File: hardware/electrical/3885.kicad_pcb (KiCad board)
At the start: 4 copper layers, 33 x 77 mm, 115 parts, among them J1 USB_B_Micro, J2 TC2030, J3 Micro_SD_Card_Det1, J4 JST-PH, J5 FFC, J6 2.54mm, Q1 AO3400A, Q2 AO3400A, Q3 AO3401A, Q4 AO3401A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

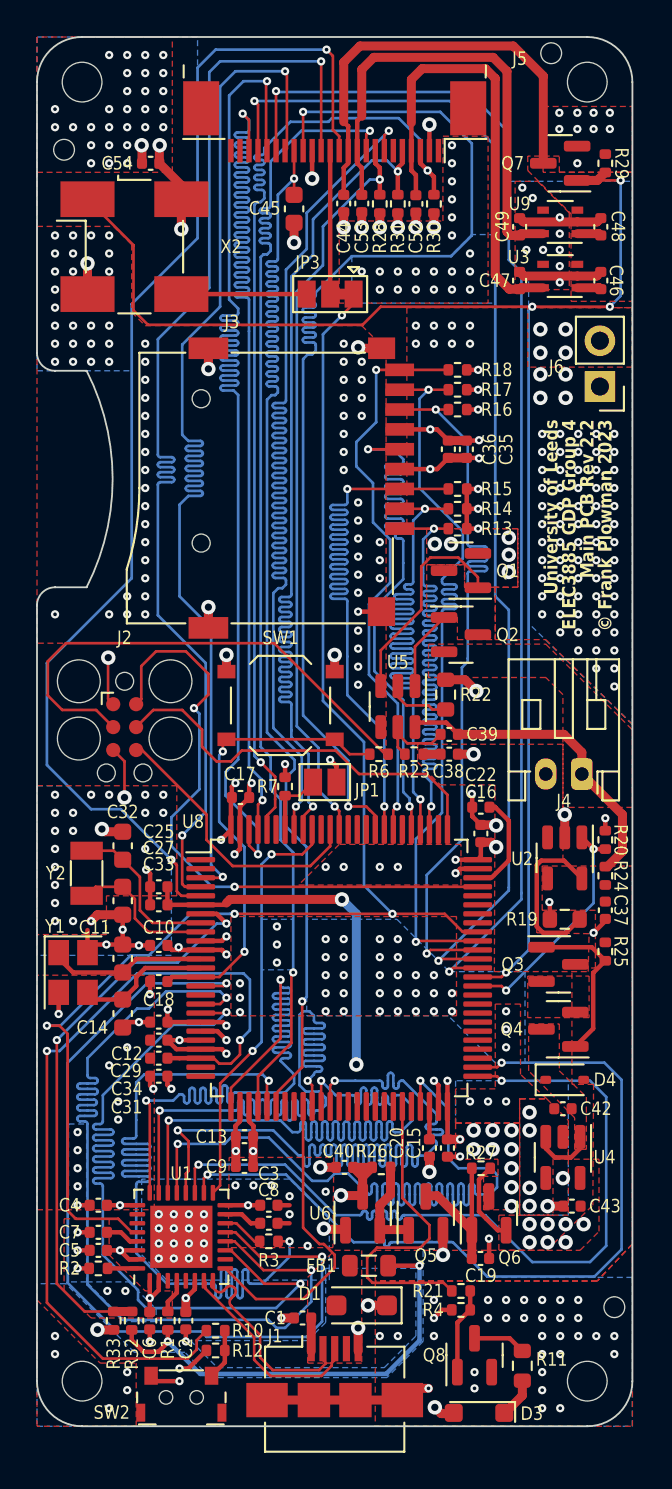
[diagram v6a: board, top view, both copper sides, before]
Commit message: JLCPCB position and rotation adjustments
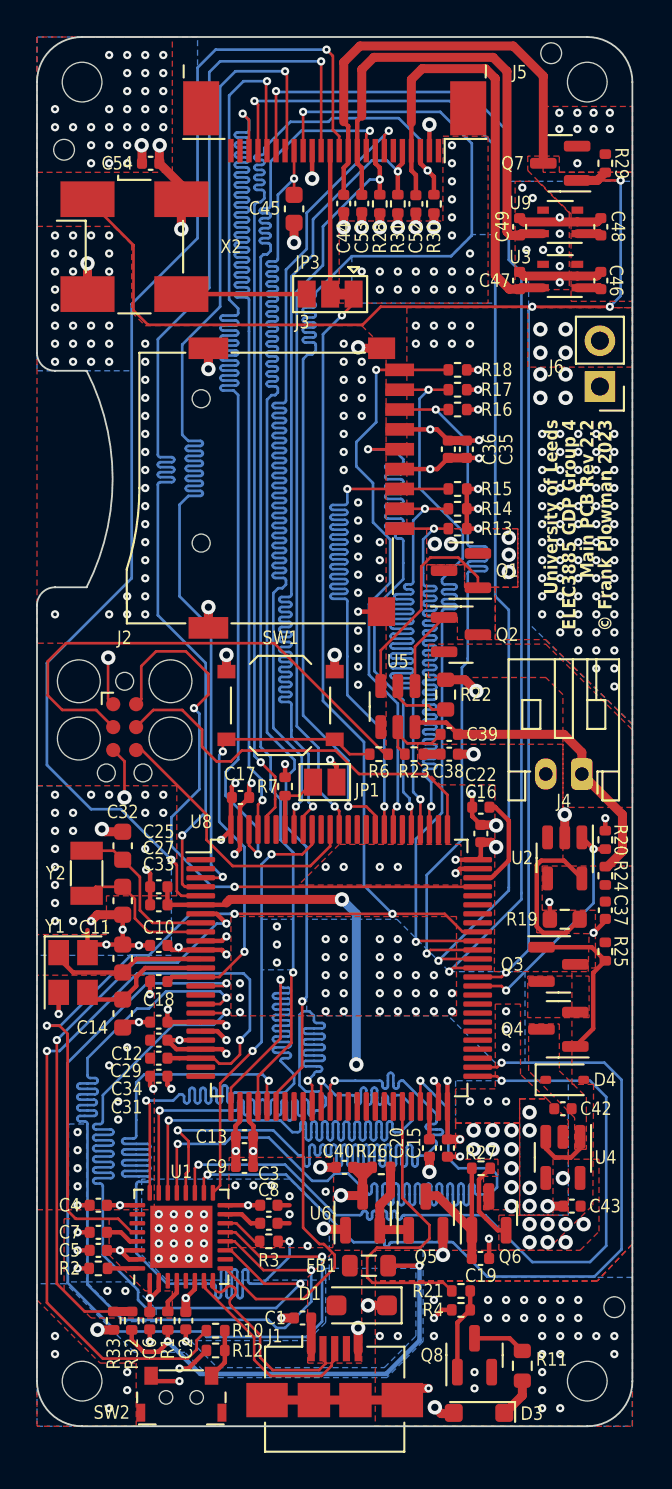
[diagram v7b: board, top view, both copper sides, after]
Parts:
- Q1, Q2, Q3, Q4, Q5, Q6, Q7, Q8, U6: footprint Package_TO_SOT_SMD:SOT-23 -> 3885:JLC_SOT-23
- U1: footprint Package_DFN_QFN:QFN-32-1EP_5x5mm_P0.5mm_EP3.45x3.45mm -> 3885:JLC_QFN-32-1EP_5x5mm_P0.5mm_EP3.45x3.45mm
- U2, U4: footprint Package_TO_SOT_SMD:SOT-23-5 -> 3885:JLC_SOT-23-5
- U3, U9: footprint Package_TO_SOT_SMD:SOT-353_SC-70-5 -> 3885:JLC_SOT-353_SC-70-5
- U5: footprint Package_TO_SOT_SMD:SOT-23-6 -> 3885:JLC_SOT-23-6
- U8: footprint Package_QFP:LQFP-100_14x14mm_P0.5mm -> 3885:JLC_LQFP-100_14x14mm_P0.5mm
- moved J3 3.90 mm to (146.7, 91.5)
- moved J5 0.75 mm to (148.5, 72.0)
- turned Q1 to 0 degrees
- turned Q2 to 180 degrees
- turned Q3 to 180 degrees
- turned Q4 to 0 degrees
- turned Q5 to -90 degrees
- turned Q6 to -90 degrees
- turned Q7 to 0 degrees
- turned Q8 to -90 degrees
- turned U1 to 0 degrees
- turned U2 to 180 degrees
- turned U3 to 90 degrees
- turned U4 to 180 degrees
- turned U5 to 180 degrees
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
